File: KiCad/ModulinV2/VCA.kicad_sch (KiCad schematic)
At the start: 21 parts, among them IC38 TL072HIDR, IC39 AS3360D

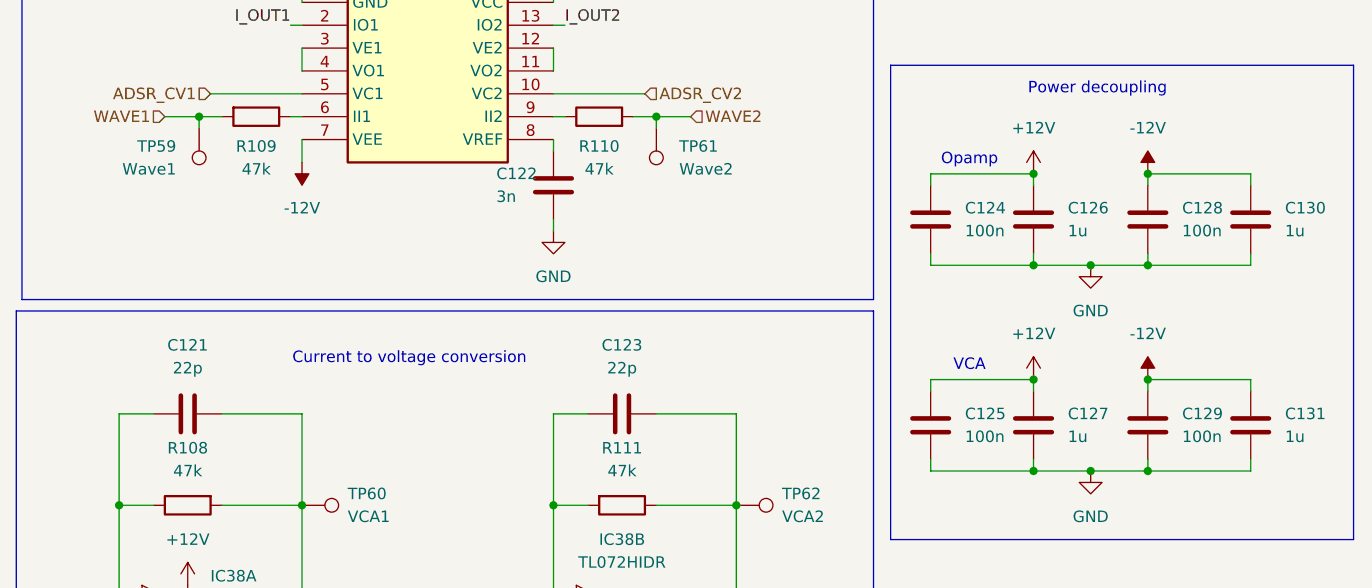
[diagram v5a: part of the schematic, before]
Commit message: Layed out Interface and PWR components and started with MCU layout
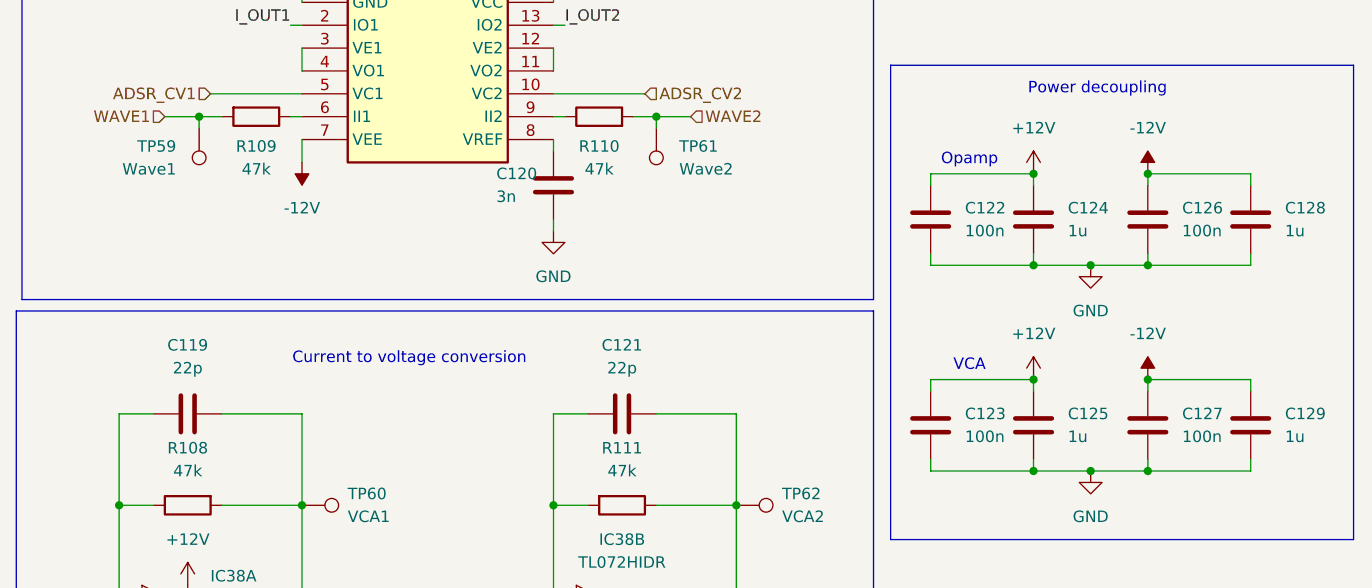
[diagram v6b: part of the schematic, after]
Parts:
- renumbered C121 to C119, C122 to C120, C123 to C121, C124 to C122, C125 to C123, C126 to C124, C127 to C125, C128 to C126, C129 to C127, C130 to C128, C131 to C129
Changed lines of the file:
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@@
 		(dnp no)
 		(fields_autoplaced yes)
-		(property "Reference" "C127"
+		(property "Reference" "C125"
 			(at 196.85 107.9499 0)
 			(effects
@@
 			(project "ModulinV2"
 				(path "/c6b34a57-3941-4b56-8b80-1848c7f41082/a5a8abcc-50bb-4382-96d0-cbdb724bb6e9"
-					(reference "C127")
+					(reference "C125")
 					(unit 1)
 				)
@@
 		(dnp no)
 		(fields_autoplaced yes)
-		(property "Reference" "C131"
+		(property "Reference" "C129"
 			(at 220.98 107.9499 0)
 			(effects
@@
 			(project "ModulinV2"
 				(path "/c6b34a57-3941-4b56-8b80-1848c7f41082/a5a8abcc-50bb-4382-96d0-cbdb724bb6e9"
-					(reference "C131")
+					(reference "C129")
 					(unit 1)
 				)
@@
 		(dnp no)
 		(fields_autoplaced yes)
-		(property "Reference" "C124"
+		(property "Reference" "C122"
 			(at 185.42 85.0899 0)
 			(effects
@@
 			(project "ModulinV2"
 				(path "/c6b34a57-3941-4b56-8b80-1848c7f41082/a5a8abcc-50bb-4382-96d0-cbdb724bb6e9"
-					(reference "C124")
+					(reference "C122")
 					(unit 1)
 				)
@@
 		(dnp no)
 		(fields_autoplaced yes)
-		(property "Reference" "C130"
+		(property "Reference" "C128"
 			(at 220.98 85.0899 0)
 			(effects
@@
 			(project "ModulinV2"
 				(path "/c6b34a57-3941-4b56-8b80-1848c7f41082/a5a8abcc-50bb-4382-96d0-cbdb724bb6e9"
-					(reference "C130")
+					(reference "C128")
 					(unit 1)
 				)
@@
 		(dnp no)
 		(fields_autoplaced yes)
-		(property "Reference" "C125"
+		(property "Reference" "C123"
 			(at 185.42 107.9499 0)
 			(effects
@@
 			(project "ModulinV2"
 				(path "/c6b34a57-3941-4b56-8b80-1848c7f41082/a5a8abcc-50bb-4382-96d0-cbdb724bb6e9"
-					(reference "C125")
+					(reference "C123")
 					(unit 1)
 				)
@@
 		(dnp no)
 		(fields_autoplaced yes)
-		(property "Reference" "C121"
+		(property "Reference" "C119"
 			(at 99.06 100.33 90)
 			(effects
@@
 			(project ""
 				(path "/c6b34a57-3941-4b56-8b80-1848c7f41082/a5a8abcc-50bb-4382-96d0-cbdb724bb6e9"
-					(reference "C121")
+					(reference "C119")
 					(unit 1)
 				)
@@
 		(dnp no)
 		(fields_autoplaced yes)
-		(property "Reference" "C129"
+		(property "Reference" "C127"
 			(at 209.55 107.9499 0)
 			(effects
@@
 			(project "ModulinV2"
 				(path "/c6b34a57-3941-4b56-8b80-1848c7f41082/a5a8abcc-50bb-4382-96d0-cbdb724bb6e9"
-					(reference "C129")
+					(reference "C127")
 					(unit 1)
 				)
@@
 		(dnp no)
 		(fields_autoplaced yes)
-		(property "Reference" "C128"
+		(property "Reference" "C126"
 			(at 209.55 85.0899 0)
 			(effects
@@
 			(project "ModulinV2"
 				(path "/c6b34a57-3941-4b56-8b80-1848c7f41082/a5a8abcc-50bb-4382-96d0-cbdb724bb6e9"
-					(reference "C128")
+					(reference "C126")
 					(unit 1)
 				)
@@
 		(on_board yes)
 		(dnp no)
-		(property "Reference" "C122"
+		(property "Reference" "C120"
 			(at 133.35 81.28 0)
 			(effects
@@
 			(project ""
 				(path "/c6b34a57-3941-4b56-8b80-1848c7f41082/a5a8abcc-50bb-4382-96d0-cbdb724bb6e9"
-					(reference "C122")
+					(reference "C120")
 					(unit 1)
 				)
@@
 		(dnp no)
 		(fields_autoplaced yes)
-		(property "Reference" "C123"
+		(property "Reference" "C121"
 			(at 147.32 100.33 90)
 			(effects
@@
 			(project ""
 				(path "/c6b34a57-3941-4b56-8b80-1848c7f41082/a5a8abcc-50bb-4382-96d0-cbdb724bb6e9"
-					(reference "C123")
+					(reference "C121")
 					(unit 1)
 				)
@@
 		(dnp no)
 		(fields_autoplaced yes)
-		(property "Reference" "C126"
+		(property "Reference" "C124"
 			(at 196.85 85.0899 0)
 			(effects
@@
 			(project "ModulinV2"
 				(path "/c6b34a57-3941-4b56-8b80-1848c7f41082/a5a8abcc-50bb-4382-96d0-cbdb724bb6e9"
-					(reference "C126")
-					(unit 1)
-				)
+					(reference "C124")
+					(unit 1)
+				)

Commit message: Completed tuning & mod wheel layouts
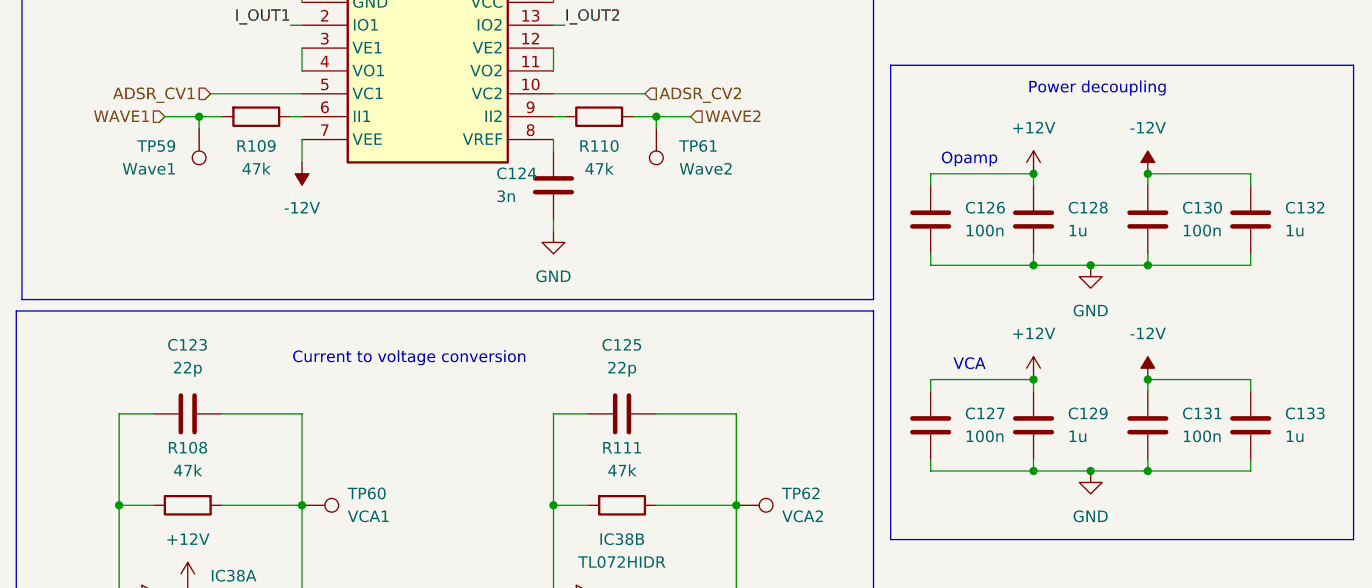
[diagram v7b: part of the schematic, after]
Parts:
- renumbered C119 to C123, C120 to C124, C121 to C125, C122 to C126, C123 to C127, C124 to C128, C125 to C129, C126 to C130, C127 to C131, C128 to C132, C129 to C133
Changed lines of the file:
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@@
 		(dnp no)
 		(fields_autoplaced yes)
-		(property "Reference" "#PWR0275"
+		(property "Reference" "#PWR0278"
 			(at 199.39 120.65 0)
 			(effects
@@
 			(project "ModulinV2"
 				(path "/c6b34a57-3941-4b56-8b80-1848c7f41082/a5a8abcc-50bb-4382-96d0-cbdb724bb6e9"
-					(reference "#PWR0275")
+					(reference "#PWR0278")
 					(unit 1)
 				)
@@
 		(dnp no)
 		(fields_autoplaced yes)
-		(property "Reference" "C125"
+		(property "Reference" "C129"
 			(at 196.85 107.9499 0)
 			(effects
@@
 			(project "ModulinV2"
 				(path "/c6b34a57-3941-4b56-8b80-1848c7f41082/a5a8abcc-50bb-4382-96d0-cbdb724bb6e9"
-					(reference "C125")
+					(reference "C129")
 					(unit 1)
 				)
@@
 		(dnp no)
 		(fields_autoplaced yes)
-		(property "Reference" "#PWR0269"
+		(property "Reference" "#PWR0272"
 			(at 139.7 63.5 0)
 			(effects
@@
 			(project ""
 				(path "/c6b34a57-3941-4b56-8b80-1848c7f41082/a5a8abcc-50bb-4382-96d0-cbdb724bb6e9"
-					(reference "#PWR0269")
+					(reference "#PWR0272")
 					(unit 1)
 				)
@@
 		(dnp no)
 		(fields_autoplaced yes)
-		(property "Reference" "#PWR0265"
+		(property "Reference" "#PWR0268"
 			(at 99.06 130.81 0)
 			(effects
@@
 			(project "ModulinV2"
 				(path "/c6b34a57-3941-4b56-8b80-1848c7f41082/a5a8abcc-50bb-4382-96d0-cbdb724bb6e9"
-					(reference "#PWR0265")
+					(reference "#PWR0268")
 					(unit 1)
 				)
@@
 		(dnp no)
 		(fields_autoplaced yes)
-		(property "Reference" "#PWR0264"
+		(property "Reference" "#PWR0267"
 			(at 91.44 142.24 0)
 			(effects
@@
 			(project ""
 				(path "/c6b34a57-3941-4b56-8b80-1848c7f41082/a5a8abcc-50bb-4382-96d0-cbdb724bb6e9"
-					(reference "#PWR0264")
+					(reference "#PWR0267")
 					(unit 1)
 				)
@@
 		(dnp no)
 		(fields_autoplaced yes)
-		(property "Reference" "#PWR0270"
+		(property "Reference" "#PWR0273"
 			(at 139.7 93.98 0)
 			(effects
@@
 			(project ""
 				(path "/c6b34a57-3941-4b56-8b80-1848c7f41082/a5a8abcc-50bb-4382-96d0-cbdb724bb6e9"
-					(reference "#PWR0270")
+					(reference "#PWR0273")
 					(unit 1)
 				)
@@
 		(dnp no)
 		(fields_autoplaced yes)
-		(property "Reference" "C129"
+		(property "Reference" "C133"
 			(at 220.98 107.9499 0)
 			(effects
@@
 			(project "ModulinV2"
 				(path "/c6b34a57-3941-4b56-8b80-1848c7f41082/a5a8abcc-50bb-4382-96d0-cbdb724bb6e9"
-					(reference "C129")
+					(reference "C133")
 					(unit 1)
 				)
@@
 		(dnp no)
 		(fields_autoplaced yes)
-		(property "Reference" "#PWR0273"
+		(property "Reference" "#PWR0276"
 			(at 193.04 107.95 0)
 			(effects
@@
 			(project "ModulinV2"
 				(path "/c6b34a57-3941-4b56-8b80-1848c7f41082/a5a8abcc-50bb-4382-96d0-cbdb724bb6e9"
-					(reference "#PWR0273")
+					(reference "#PWR0276")
 					(unit 1)
 				)
@@
 		(dnp no)
 		(fields_autoplaced yes)
-		(property "Reference" "#PWR0267"
+		(property "Reference" "#PWR0270"
 			(at 111.76 76.2 0)
 			(effects
@@
 			(project ""
 				(path "/c6b34a57-3941-4b56-8b80-1848c7f41082/a5a8abcc-50bb-4382-96d0-cbdb724bb6e9"
-					(reference "#PWR0267")
+					(reference "#PWR0270")
 					(unit 1)
 				)
@@
 		(dnp no)
 		(fields_autoplaced yes)
-		(property "Reference" "#PWR0274"
+		(property "Reference" "#PWR0277"
 			(at 199.39 97.79 0)
 			(effects
@@
 			(project "ModulinV2"
 				(path "/c6b34a57-3941-4b56-8b80-1848c7f41082/a5a8abcc-50bb-4382-96d0-cbdb724bb6e9"
-					(reference "#PWR0274")
+					(reference "#PWR0277")
 					(unit 1)
 				)
@@
 		(dnp no)
 		(fields_autoplaced yes)
-		(property "Reference" "#PWR0268"
+		(property "Reference" "#PWR0271"
 			(at 115.57 59.69 0)
 			(effects
@@
 			(project ""
 				(path "/c6b34a57-3941-4b56-8b80-1848c7f41082/a5a8abcc-50bb-4382-96d0-cbdb724bb6e9"
-					(reference "#PWR0268")
+					(reference "#PWR0271")
 					(unit 1)
 				)
@@
 		(dnp no)
 		(fields_autoplaced yes)
-		(property "Reference" "C122"
+		(property "Reference" "C126"
 			(at 185.42 85.0899 0)
 			(effects
@@
 			(project "ModulinV2"
 				(path "/c6b34a57-3941-4b56-8b80-1848c7f41082/a5a8abcc-50bb-4382-96d0-cbdb724bb6e9"
-					(reference "C122")
+					(reference "C126")
 					(unit 1)
 				)
@@
 		(dnp no)
 		(fields_autoplaced yes)
-		(property "Reference" "C128"
+		(property "Reference" "C132"
 			(at 220.98 85.0899 0)
 			(effects
@@
 			(project "ModulinV2"
 				(path "/c6b34a57-3941-4b56-8b80-1848c7f41082/a5a8abcc-50bb-4382-96d0-cbdb724bb6e9"
-					(reference "C128")
+					(reference "C132")
 					(unit 1)
 				)
@@
 		(dnp no)
 		(fields_autoplaced yes)
-		(property "Reference" "C123"
+		(property "Reference" "C127"
 			(at 185.42 107.9499 0)
 			(effects
@@
 			(project "ModulinV2"
 				(path "/c6b34a57-3941-4b56-8b80-1848c7f41082/a5a8abcc-50bb-4382-96d0-cbdb724bb6e9"
-					(reference "C123")
+					(reference "C127")
 					(unit 1)
 				)
@@
 		(dnp no)
 		(fields_autoplaced yes)
-		(property "Reference" "C119"
+		(property "Reference" "C123"
 			(at 99.06 100.33 90)
 			(effects
@@
 			(project ""
 				(path "/c6b34a57-3941-4b56-8b80-1848c7f41082/a5a8abcc-50bb-4382-96d0-cbdb724bb6e9"
-					(reference "C119")
+					(reference "C123")
 					(unit 1)
 				)
@@
 		(dnp no)
 		(fields_autoplaced yes)
-		(property "Reference" "#PWR0272"
+		(property "Reference" "#PWR0275"
 			(at 193.04 85.09 0)
 			(effects
@@
 			(project "ModulinV2"
 				(path "/c6b34a57-3941-4b56-8b80-1848c7f41082/a5a8abcc-50bb-4382-96d0-cbdb724bb6e9"
-					(reference "#PWR0272")
+					(reference "#PWR0275")
 					(unit 1)
 				)
@@
 		(dnp no)
 		(fields_autoplaced yes)
-		(property "Reference" "#PWR0266"
+		(property "Reference" "#PWR0269"
 			(at 99.06 133.35 0)
 			(effects
@@
 			(project "ModulinV2"
 				(path "/c6b34a57-3941-4b56-8b80-1848c7f41082/a5a8abcc-50bb-4382-96d0-cbdb724bb6e9"
-					(reference "#PWR0266")
+					(reference "#PWR0269")
 					(unit 1)
 				)
@@
 		(dnp no)
 		(fields_autoplaced yes)
-		(property "Reference" "C127"
+		(property "Reference" "C131"
 			(at 209.55 107.9499 0)
 			(effects
@@
 			(project "ModulinV2"
 				(path "/c6b34a57-3941-4b56-8b80-1848c7f41082/a5a8abcc-50bb-4382-96d0-cbdb724bb6e9"
-					(reference "C127")
+					(reference "C131")
 					(unit 1)
 				)
@@
 		(dnp no)
 		(fields_autoplaced yes)
-		(property "Reference" "#PWR0277"
+		(property "Reference" "#PWR0280"
 			(at 205.74 107.95 0)
 			(effects
@@
 			(project "ModulinV2"
 				(path "/c6b34a57-3941-4b56-8b80-1848c7f41082/a5a8abcc-50bb-4382-96d0-cbdb724bb6e9"
-					(reference "#PWR0277")
+					(reference "#PWR0280")
 					(unit 1)
 				)
@@
 		(dnp no)
 		(fields_autoplaced yes)
-		(property "Reference" "C126"
+		(property "Reference" "C130"
 			(at 209.55 85.0899 0)
 			(effects
@@
 			(project "ModulinV2"
 				(path "/c6b34a57-3941-4b56-8b80-1848c7f41082/a5a8abcc-50bb-4382-96d0-cbdb724bb6e9"
-					(reference "C126")
+					(reference "C130")
 					(unit 1)
 				)
@@
 		(dnp no)
 		(fields_autoplaced yes)
-		(property "Reference" "#PWR0276"
+		(property "Reference" "#PWR0279"
 			(at 205.74 85.09 0)
 			(effects
@@
 			(project "ModulinV2"
 				(path "/c6b34a57-3941-4b56-8b80-1848c7f41082/a5a8abcc-50bb-4382-96d0-cbdb724bb6e9"
-					(reference "#PWR0276")
+					(reference "#PWR0279")
 					(unit 1)
 				)
@@
 		(on_board yes)
 		(dnp no)
-		(property "Reference" "C120"
+		(property "Reference" "C124"
 			(at 133.35 81.28 0)
 			(effects
@@
 			(project ""
 				(path "/c6b34a57-3941-4b56-8b80-1848c7f41082/a5a8abcc-50bb-4382-96d0-cbdb724bb6e9"
-					(reference "C120")
+					(reference "C124")
 					(unit 1)
 				)
@@
 		(dnp no)
 		(fields_autoplaced yes)
-		(property "Reference" "#PWR0271"
+		(property "Reference" "#PWR0274"
 			(at 139.7 142.24 0)
 			(effects
@@
 			(project ""
 				(path "/c6b34a57-3941-4b56-8b80-1848c7f41082/a5a8abcc-50bb-4382-96d0-cbdb724bb6e9"
-					(reference "#PWR0271")
+					(reference "#PWR0274")
 					(unit 1)
 				)
@@
 		(dnp no)
 		(fields_autoplaced yes)
-		(property "Reference" "C121"
+		(property "Reference" "C125"
 			(at 147.32 100.33 90)
 			(effects
@@
 			(project ""
 				(path "/c6b34a57-3941-4b56-8b80-1848c7f41082/a5a8abcc-50bb-4382-96d0-cbdb724bb6e9"
-					(reference "C121")
+					(reference "C125")
 					(unit 1)
 				)
@@
 		(dnp no)
 		(fields_autoplaced yes)
-		(property "Reference" "C124"
+		(property "Reference" "C128"
 			(at 196.85 85.0899 0)
 			(effects
@@
 			(project "ModulinV2"
 				(path "/c6b34a57-3941-4b56-8b80-1848c7f41082/a5a8abcc-50bb-4382-96d0-cbdb724bb6e9"
-					(reference "C124")
-					(unit 1)
-				)
+					(reference "C128")
+					(unit 1)
+				)

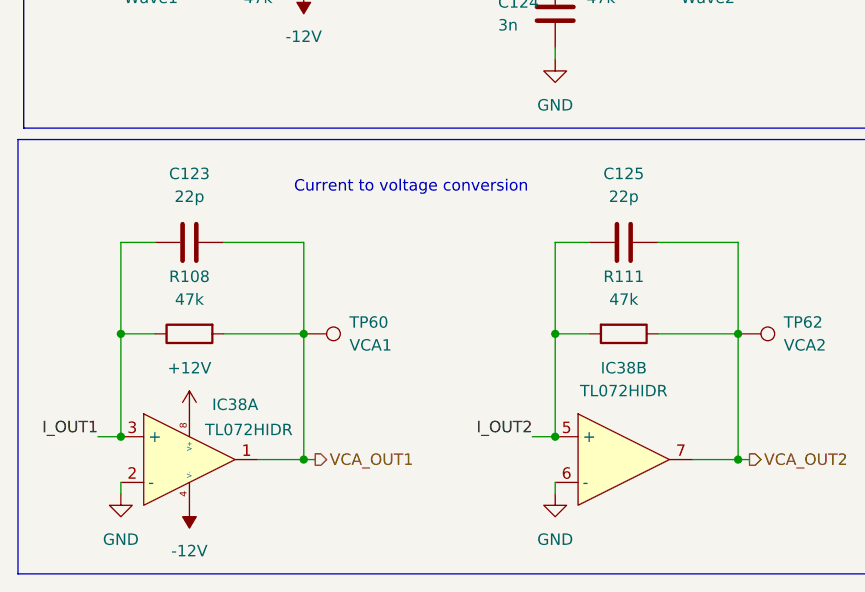
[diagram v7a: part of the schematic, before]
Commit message: Fixed schematic connections
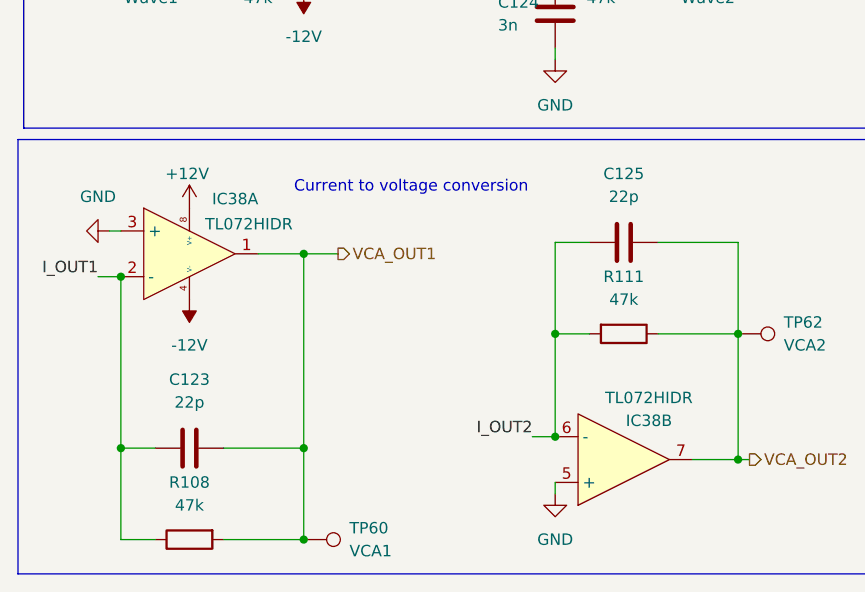
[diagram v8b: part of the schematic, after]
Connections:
- net GND: now also IC38.3 (+), IC38.5 (+); no longer IC38.2 (-), IC38.6 (-)
- net I_OUT1: now also IC38.2 (-); no longer IC38.3 (+)
- net I_OUT2: now also IC38.6 (-); no longer IC38.5 (+)
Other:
- company: (none) -> TalTech
- moved on the sheet: C123, IC38A, R108, TP60
